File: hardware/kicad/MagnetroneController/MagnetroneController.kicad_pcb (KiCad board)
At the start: 4 copper layers, 80 x 80 mm, 24 parts, among them J1 Conn_01x04, J2 DIN-5_180degree, J3 DIN-5_180degree, J4 Barrel_Jack_MountingPin, J7 Conn_02x05_Odd_Even, J8 Conn_02x13_Counter_Clockwise, SW9 SW_SPST 24V, U10 Teensy4.1, U12 6N137

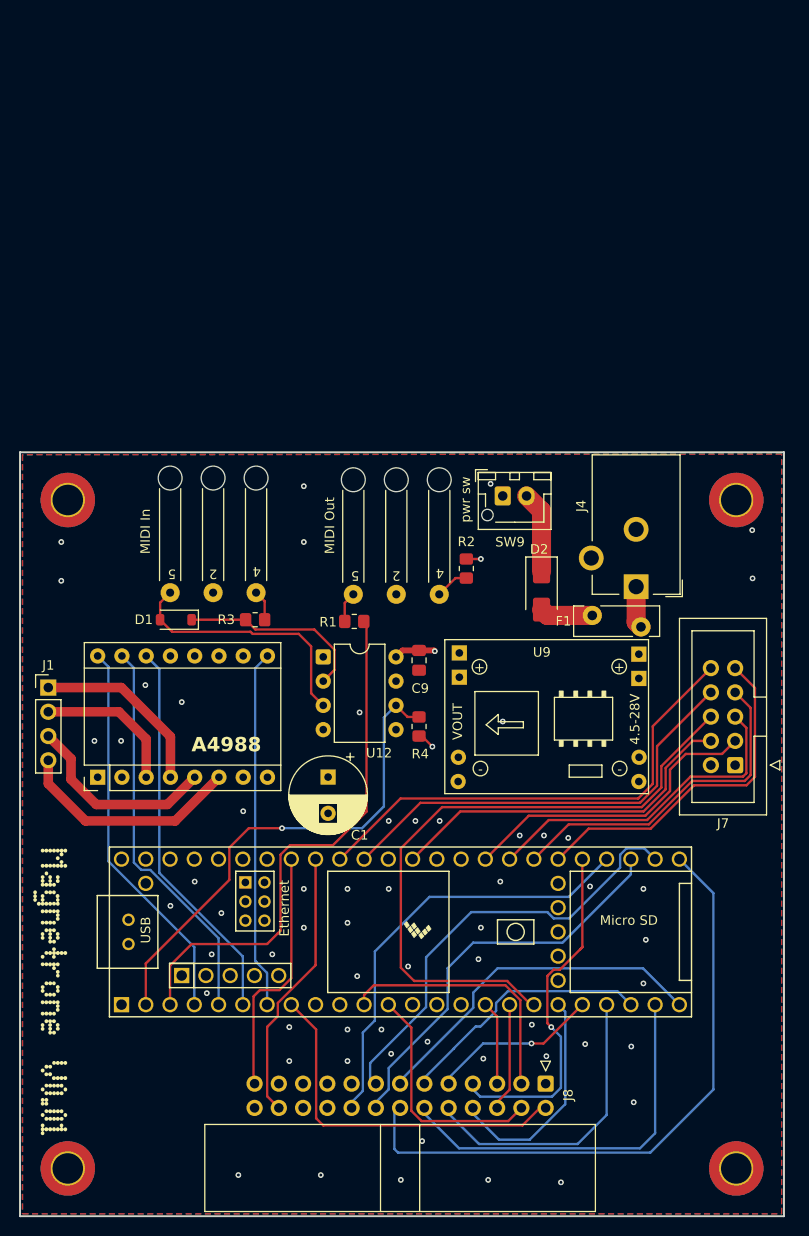
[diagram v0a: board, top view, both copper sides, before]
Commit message: chore: replace motor driver
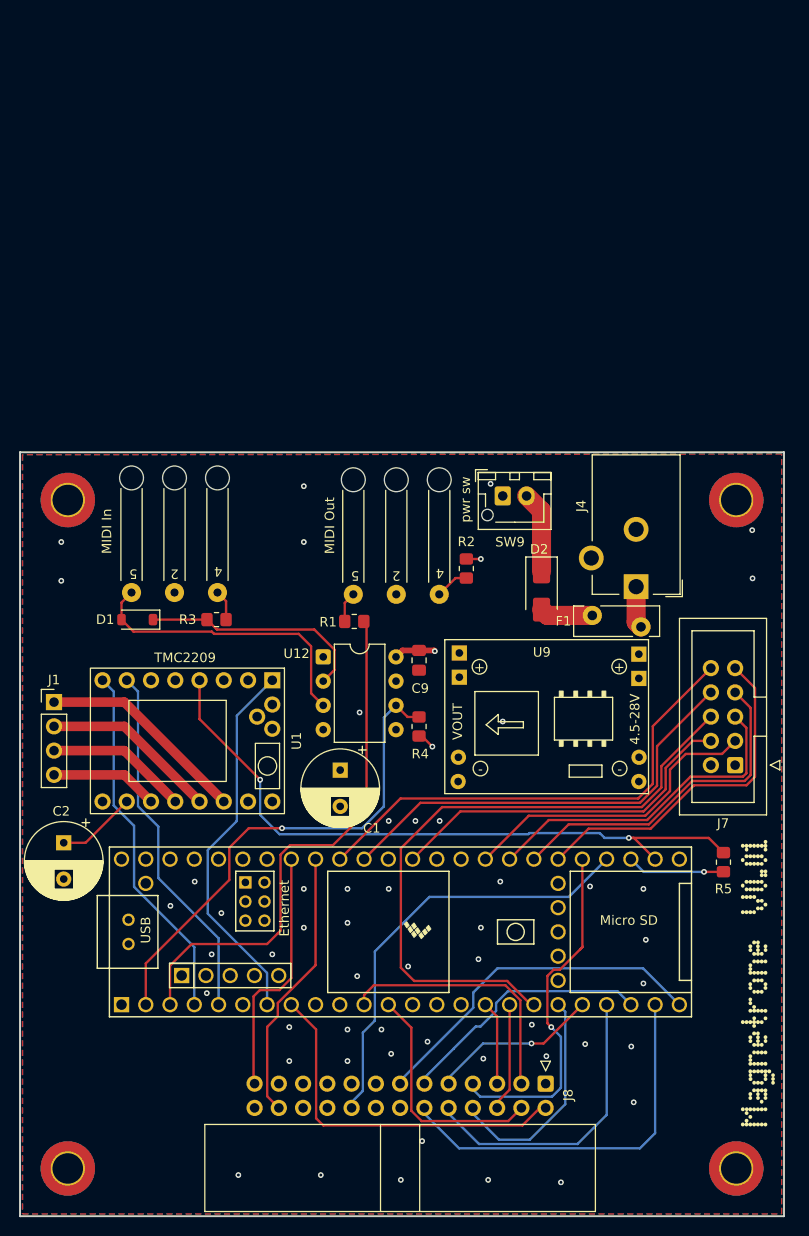
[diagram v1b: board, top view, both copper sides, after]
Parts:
- removed A1: Pololu_Breakout_A4988, Module:Pololu_Breakout-16_15.2x20.3mm
- added C2: 100uf, Capacitor_THT:CP_Radial_D8.0mm_P3.80mm, F.Cu at (55.4, 104.4)
- added R5: 1k, Resistor_SMD:R_0805_2012Metric_Pad1.20x1.40mm_HandSolder, F.Cu at (124.5, 106.4)
- added U1: TMC2209_BTT_V1.3, magnetrone:TMC2209_BTT_V1.3, F.Cu at (68.3, 93.7)
- moved D1 4.04 mm to (63.1, 81.0)
- moved R3 4.04 mm to (71.4, 81.0)
- moved J3 4.04 mm to (71.5, 78.2)
- moved J1 1.64 mm to (54.4, 89.7)
- moved C1 1.46 mm to (84.3, 96.8)
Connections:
- J1 pad 1: Net-(A1-1A) -> /motor_driver/coil_a2
- J1 pad 2: Net-(A1-1B) -> /motor_driver/coil_a1
- J1 pad 3: Net-(A1-2A) -> /motor_driver/coil_b1
- J1 pad 4: Net-(A1-2B) -> /motor_driver/coil_b2
- J8 pad 14: /mcu/encoder_aux2_a -> unconnected-(J8-Pin_14-Pad14)
- J8 pad 15: /mcu/encoder_aux2_b -> unconnected-(J8-Pin_15-Pad15)
- J8 pad 16: /mcu/encoder_aux2_btn -> unconnected-(J8-Pin_16-Pad16)
- U10 pad 25: /mcu/encoder_aux2_a -> unconnected-(U10-33_MCLK2-Pad25)
- U10 pad 26: /mcu/encoder_aux2_b -> /mcu/stepper_uart_rx
- U10 pad 27: /mcu/encoder_aux2_btn -> /mcu/stepper_uart_tx
- U10 pad 6: /mcu/stepper_sleep -> unconnected-(U10-4_BCLK2-Pad6)
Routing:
- net /mcu/stepper_uart_rx: track 0.00 -> 70.6 mm, vias 0 -> 2
- net /mcu/encoder_aux2_a: track 66.2 -> 0.00 mm
- net /mcu/encoder_aux2_b: track 46.2 -> 0.00 mm
- net /mcu/encoder_aux2_btn: track 42.8 -> 0.00 mm
- net /mcu/stepper_sleep: track 40.7 -> 0.00 mm
- net Net-(A1-2B): track 23.8 -> 0.00 mm
- net /motor_driver/coil_a2: track 0.00 -> 22.1 mm
- net Net-(A1-2A): track 20.7 -> 0.00 mm
- net Net-(A1-1A): track 19.2 -> 0.00 mm
- net /motor_driver/coil_a1: track 0.00 -> 18.5 mm
- net Net-(A1-1B): track 15.4 -> 0.00 mm
- net /motor_driver/coil_b1: track 0.00 -> 14.9 mm
- net /motor_driver/coil_b2: track 0.00 -> 11.3 mm
- net /mcu/stepper_uart_tx: track 0.00 -> 10.2 mm, vias 0 -> 1
- net +3.3V: track 3.09 -> 11.5 mm
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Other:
- board text added: "TMC2209"
- board text removed: "A4988"

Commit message: feat: cleanup
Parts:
- J8: footprint Connector_IDC:IDC-Header_2x13_P2.54mm_Horizontal -> Connector_IDC:IDC-Header_2x13_P2.54mm_Vertical
- U10: footprint teensy:Teensy41 -> magnetrone:Teensy41_AudioShield_RevD
- moved R5 34.0 mm to (90.9, 100.8), turned to 0 degrees
- moved J7 30.5 mm to (126.5, 126.7)
- moved C9 21.6 mm to (83.3, 65.8), turned to 0 degrees
- moved R4 18.4 mm to (86.9, 74.7)
- moved U12 17.4 mm to (76.7, 68.6)
- moved C2 16.3 mm to (60.2, 88.9)
- moved F1 12.4 mm to (126.6, 75.7), turned to -90 degrees
- moved C1 11.2 mm to (91.7, 88.4)
- moved U1 9.35 mm to (75.2, 87.4)
- moved J1 9.15 mm to (53.8, 80.5)
- moved U9 7.70 mm to (113.0, 93.0)
- moved U10 7.68 mm to (83.2, 111.9)
- moved J8 7.61 mm to (105.8, 137.2)
- moved D1 7.18 mm to (58.4, 75.6), turned to -90 degrees
- moved R3 6.51 mm to (73.7, 74.9), turned to 90 degrees
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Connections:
- U10 pad 18: /mcu/hall7 -> /mcu/hall8
- U10 pad 19: /mcu/volume_encoder_a -> /mcu/volume_encoder_b
- U10 pad 20: /mcu/volume_encoder_b -> /mcu/volume_encoder_btn
- U10 pad 21: /mcu/volume_encoder_btn -> /mcu/volume_encoder_a
- U10 pad 32: /mcu/hall2 -> /mcu/hall5
- U10 pad 33: /mcu/hall1 -> /mcu/hall6
- U10 pad 36: /mcu/hall8 -> /mcu/hall2
- U10 pad 38: /mcu/hall6 -> /mcu/hall7
- U10 pad 39: /mcu/hall5 -> /mcu/hall1
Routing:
- net +5V: track 133.9 -> 214.8 mm, vias 1 -> 0
- net /mcu/hall1: track 32.6 -> 57.9 mm
- net /mcu/menu_encoder_b: track 26.7 -> 47.5 mm, vias 0 -> 1
- net /mcu/midi_rx: track 52.1 -> 70.3 mm, vias 1 -> 0
- net /mcu/menu_encoder_a: track 37.5 -> 54.2 mm, vias 0 -> 1
- net /mcu/aux1_btn: track 45.9 -> 61.6 mm
- net /mcu/hall7: track 67.2 -> 51.8 mm
- net /mcu/menu_encoder_btn: track 24.7 -> 39.7 mm
- net /mcu/hall2: track 34.9 -> 49.2 mm
- net /mcu/stepper_uart_rx: track 70.6 -> 56.5 mm, vias 2 -> 0
- net /mcu/encoder_aux1_a: track 27.3 -> 40.8 mm, vias 0 -> 1
- net /mcu/speed_encoder_a: track 8.78 -> 21.9 mm
- net /mcu/hall5: track 50.7 -> 38.0 mm
- net /power/FUSE_DIODE_24V: track 5.57 -> 18.0 mm
- net /mcu/speed_encoder_b: track 11.6 -> 23.8 mm
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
